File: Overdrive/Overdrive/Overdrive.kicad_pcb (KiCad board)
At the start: 4 copper layers, 51.5 x 32 mm, 42 parts, among them J1 Conn_02x08_Odd_Even, Q1 2N3904, Q2 2N3904, U1 TL071HIDBVR, U2 AD5160, U3 TL071HIDBVR, U4 ADP7118AUJZ-4.5-R7, U5 AD8400ARZ1, U6 TL071HIDBVR

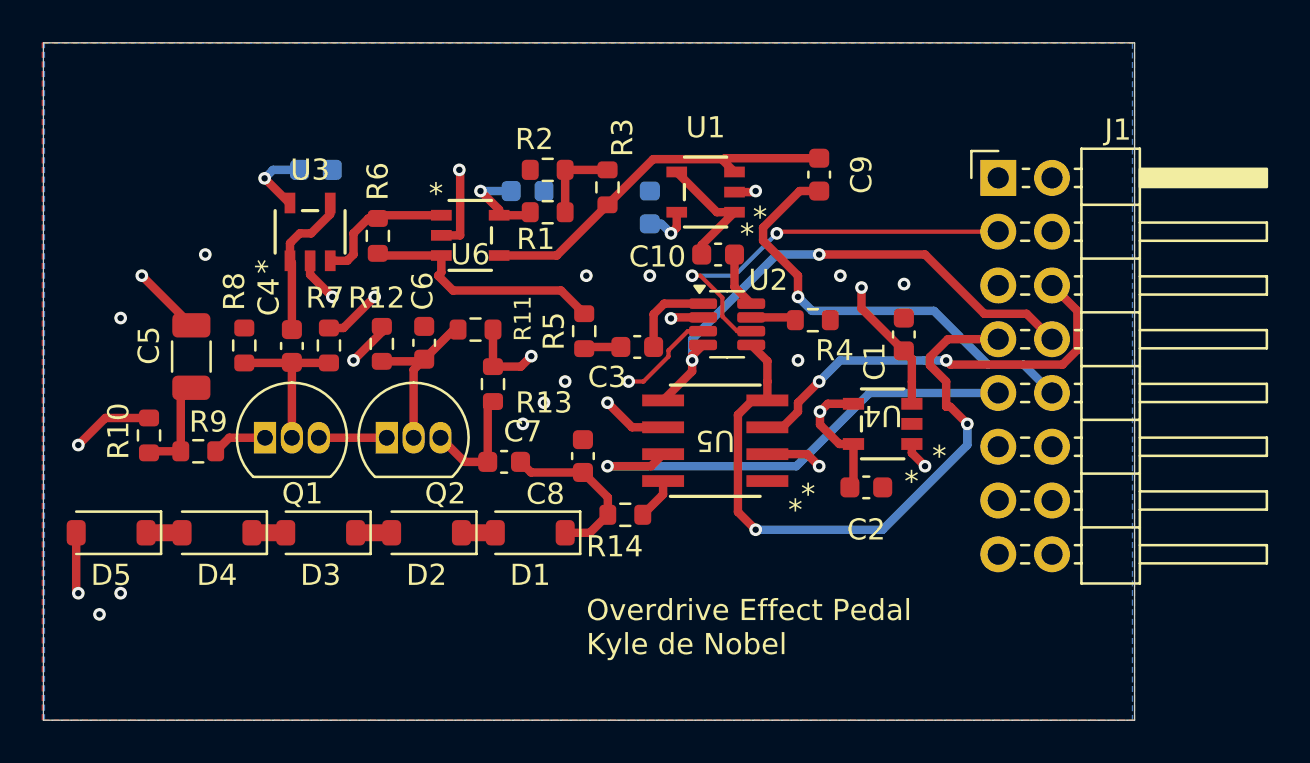
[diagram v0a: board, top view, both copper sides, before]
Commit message: board fixes for Overdrive based off of Joseph's reviews
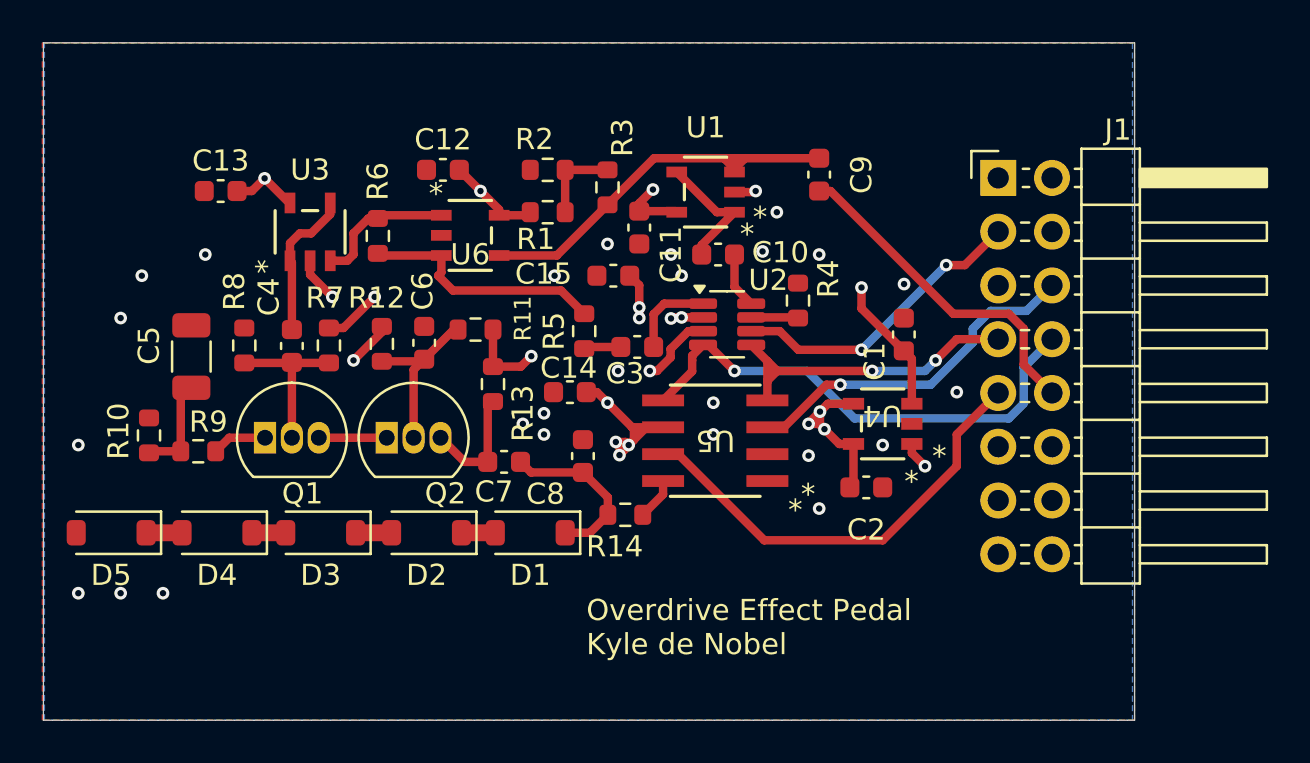
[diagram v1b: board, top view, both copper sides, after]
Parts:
- added C14: 1u, Capacitor_SMD:C_0603_1608Metric, F.Cu at (185.2, 54.5)
- added C15: 1u, Capacitor_SMD:C_0603_1608Metric, F.Cu at (187.3, 49.0)
- C11, C12, C13: moved to F.Cu
- moved C13 20.3 mm to (168.7, 45.0), turned to 0 degrees
- moved C11 15.5 mm to (188.5, 46.7), turned to 90 degrees
- moved C12 4.12 mm to (179.2, 44.0), turned to 0 degrees
- moved R4 1.16 mm to (196.0, 50.2), turned to 90 degrees
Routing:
- net GND: track 26.8 -> 8.95 mm, vias 21 -> 29
- net /MOSI: track 30.6 -> 16.1 mm
- net 5V: track 11.1 -> 21.1 mm, vias 3 -> 11
- net /GUITAR_IN: track 21.2 -> 15.9 mm, vias 1 -> 0
- net /CS2: track 19.6 -> 14.3 mm
- net /CS0: track 20.1 -> 16.6 mm, vias 2 -> 1
- net /GUITAR_OUT: track 22.8 -> 21.3 mm, vias 1 -> 0
- net 6V: track 17.9 -> 19.2 mm
- net /SPI_CLK: track 24.7 -> 23.9 mm, vias 2 -> 1
